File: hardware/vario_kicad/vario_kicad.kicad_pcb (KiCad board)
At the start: 4 copper layers, 70 x 50 mm, 94 parts, among them Q1 NMOS, Q2 PMOS, U2 BME280, U3 W25Q128JVS, U4 USB C connector, U5 STM32L072CBTx, Y1 Crystal, Y2 Crystal_GND24

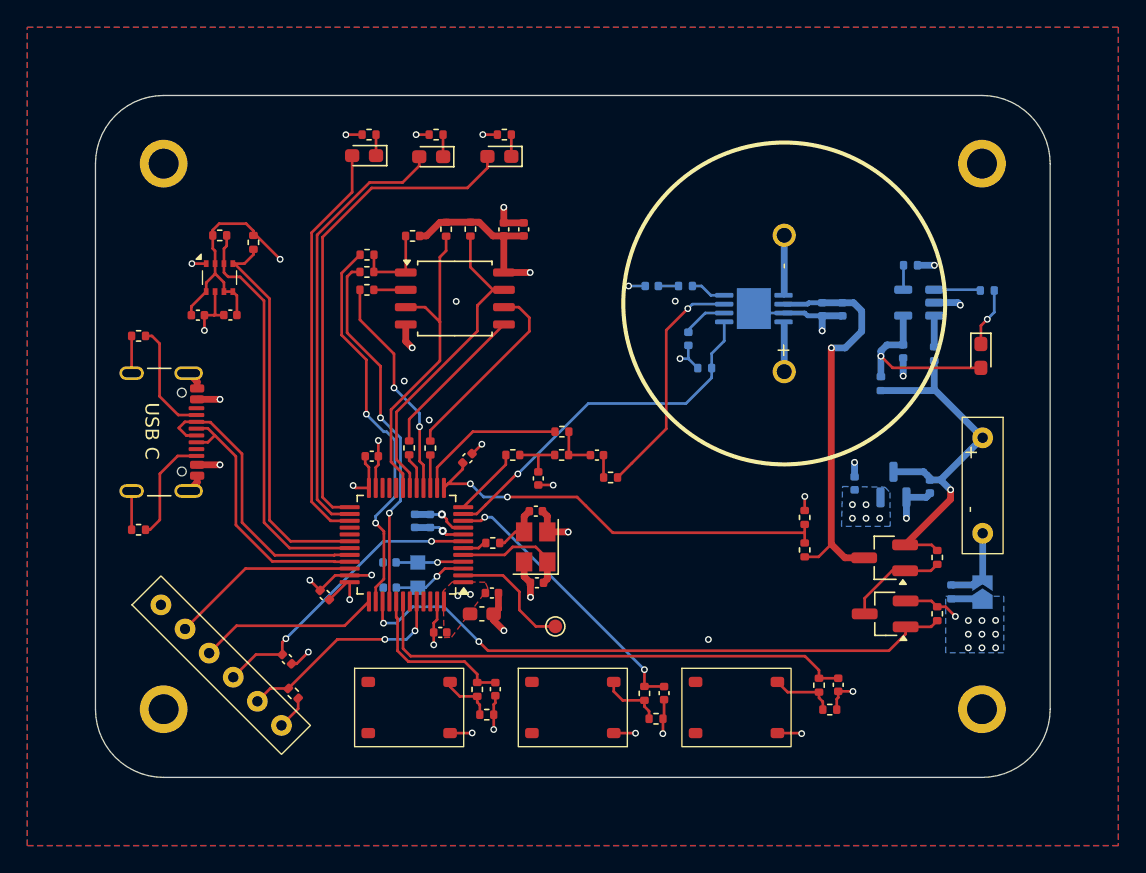
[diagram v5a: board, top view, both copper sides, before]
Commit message: modify silkscreen
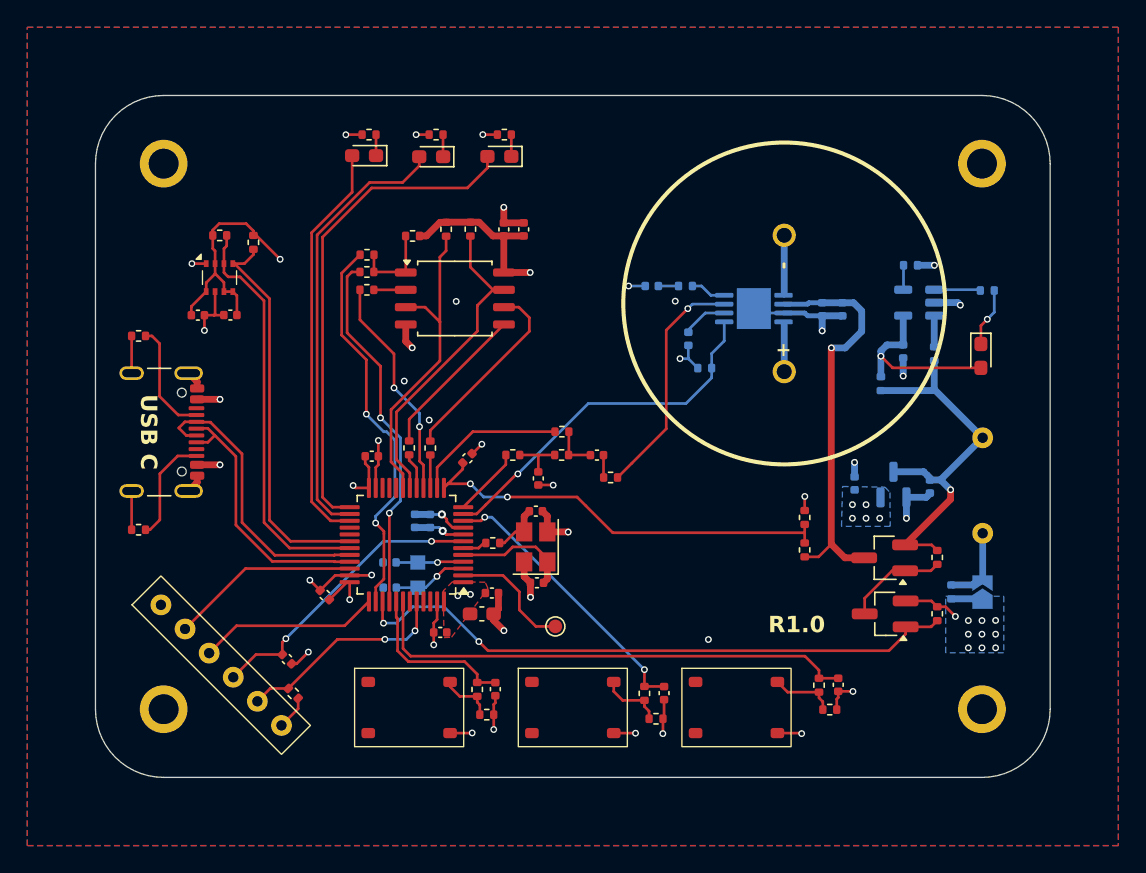
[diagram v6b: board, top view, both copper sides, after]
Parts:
- BT2: moved to B.Cu
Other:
- board text added: "R1.0"
- board text added: "github.com/vasilNnikolov/vario"
- board text removed: "github.com/vasilNnikolov/vario R1.0"
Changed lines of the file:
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@@
 				(font
 					(size 1 1)
-					(thickness 0.1)
+					(thickness 0.2)
+					(bold yes)
 				)
 				(justify left bottom)
@@
 				(font
 					(size 1 1)
-					(thickness 0.1)
+					(thickness 0.2)
+					(bold yes)
 				)
 				(justify left bottom)
@@
 		(tags "capacitor")
 		(property "Reference" "C13"
-			(at 0 -1.16 360)
+			(at 0 -1.16 0)
 			(layer "F.SilkS")
 			(hide yes)
@@
 		)
 		(property "Value" "12.5pF"
-			(at 0 1.16 360)
+			(at 0 1.16 0)
 			(layer "F.Fab")
 			(effects
@@
 		)
 		(fp_text user "${REFERENCE}"
-			(at 0 0 360)
+			(at 0 0 0)
 			(layer "F.Fab")
 			(effects
@@
 		(tags "capacitor")
 		(property "Reference" "C20"
-			(at 0 -1.16 360)
+			(at 0 -1.16 0)
 			(layer "F.SilkS")
 			(hide yes)
@@
 		)
 		(property "Value" "12.5pF"
-			(at 0 1.16 360)
+			(at 0 1.16 0)
 			(layer "F.Fab")
 			(effects
@@
 		)
 		(fp_text user "${REFERENCE}"
-			(at 0 0 360)
+			(at 0 0 0)
 			(layer "F.Fab")
 			(effects
@@
 		)
 		(fp_text user "USB C"
-			(at -2.5 8.5 -90)
+			(at -3.1 8.85 -90)
 			(unlocked yes)
 			(layer "F.SilkS")
 			(effects
 				(font
-					(size 1 1)
-					(thickness 0.1)
+					(size 1.2 1.2)
+					(thickness 0.2)
+					(bold yes)
 				)
 				(justify left bottom)
@@
 		)
 		(fp_text user "${REFERENCE}"
-			(at 0 2.5 -90)
+			(at 0 -2.5 -90)
 			(unlocked yes)
 			(layer "F.Fab")
@@
 		)
 		(fp_text user "${REFERENCE}"
-			(at 0 -2.5 -90)
+			(at 0 2.5 -90)
 			(unlocked yes)
 			(layer "F.Fab")
@@
 		)
 	)
-	(footprint "symbol_lib:battery_th"
-		(layer "F.Cu")
-		(at 165.05 128.6 -90)
-		(property "Reference" "BT2"
-			(at 0 -13.5 -90)
-			(unlocked yes)
-			(layer "F.SilkS")
-			(hide yes)
-			(effects
-				(font
-					(size 1 1)
-					(thickness 0.1)
-				)
-			)
-		)
-		(property "Value" "Battery_Cell"
-			(at 0 -12 -90)
-			(unlocked yes)
-			(layer "F.Fab")
-			(effects
-				(font
-					(size 1 1)
-					(thickness 0.15)
-				)
-			)
-		)
-		(property "Footprint" "symbol_lib:battery_th"
-			(at 0 -13 -90)
-			(unlocked yes)
-			(layer "F.Fab")
-			(hide yes)
-			(effects
-				(font
-					(size 1 1)
-					(thickness 0.15)
-				)
-			)
-		)
-		(property "Datasheet" ""
-			(at 0 -13 -90)
-			(unlocked yes)
-			(layer "F.Fab")
-			(hide yes)
-			(effects
-				(font
-					(size 1 1)
-					(thickness 0.15)
-				)
-			)
-		)
-		(property "Description" "Single-cell battery"
-			(at 0 -13 -90)
-			(unlocked yes)
-			(layer "F.Fab")
-			(hide yes)
-			(effects
-				(font
-					(size 1 1)
-					(thickness 0.15)
-				)
-			)
-		)
-		(property "Sim.Pins" ""
-			(at 0 0 -90)
-			(unlocked yes)
-			(layer "F.Fab")
-			(hide yes)
-			(effects
-				(font
-					(size 1 1)
-					(thickness 0.15)
-				)
-			)
-		)
-		(sheetname "power")
-		(sheetfile "power.kicad_sch")
-		(attr through_hole)
-		(fp_rect
-			(start -5 -1.5)
-			(end 5 1.5)
-			(stroke
-				(width 0.1)
-				(type default)
-			)
-			(fill none)
-			(layer "F.SilkS")
-		)
-		(fp_text user "+"
-			(at -3 1.4 -90)
-			(unlocked yes)
-			(layer "F.SilkS")
-			(effects
-				(font
-					(size 1 1)
-					(thickness 0.1)
-				)
-				(justify left bottom)
-			)
-		)
-		(fp_text user "-"
-			(at 1.5 1.4 -90)
-			(unlocked yes)
-			(layer "F.SilkS")
-			(effects
-				(font
-					(size 1 1)
-					(thickness 0.1)
-				)
-				(justify left bottom)
-			)
-		)
-		(fp_text user "${REFERENCE}"
-			(at 0 -10.5 -90)
-			(unlocked yes)
-			(layer "F.Fab")
-			(effects
-				(font
-					(size 1 1)
-					(thickness 0.15)
-				)
-			)
-		)
-		(pad "1" thru_hole circle
-			(at -3.5 0 270)
-			(size 1.524 1.524)
-			(drill 0.762)
-			(layers "*.Cu" "*.Mask" "In3.Cu" "In4.Cu" "In5.Cu" "In6.Cu" "In7.Cu" "In8.Cu"
-				"In9.Cu" "In10.Cu" "In11.Cu" "In12.Cu" "In13.Cu" "In14.Cu" "In15.Cu"
-				"In16.Cu" "In17.Cu" "In18.Cu" "In19.Cu" "In20.Cu" "In21.Cu" "In22.Cu"
-				"In23.Cu" "In24.Cu" "In25.Cu" "In26.Cu" "In27.Cu" "In28.Cu" "In29.Cu"
-				"In30.Cu"
-			)
-			(remove_unused_layers no)
-			(net 1 "VBATT")
-			(pinfunction "+")
-			(pintype "passive")
-		)
-		(pad "2" thru_hole circle
-			(at 3.5 0 270)
-			(size 1.524 1.524)
-			(drill 0.762)
-			(layers "*.Cu" "*.Mask" "In3.Cu" "In4.Cu" "In5.Cu" "In6.Cu" "In7.Cu" "In8.Cu"
-				"In9.Cu" "In10.Cu" "In11.Cu" "In12.Cu" "In13.Cu" "In14.Cu" "In15.Cu"
-				"In16.Cu" "In17.Cu" "In18.Cu" "In19.Cu" "In20.Cu" "In21.Cu" "In22.Cu"
-				"In23.Cu" "In24.Cu" "In25.Cu" "In26.Cu" "In27.Cu" "In28.Cu" "In29.Cu"
-				"In30.Cu"
-			)
-			(remove_unused_layers no)
-			(net 58 "Net-(BT2--)")
-			(pinfunction "-")
-			(pintype "passive")
-		)
-	)
 	(footprint "Capacitor_SMD:C_0402_1005Metric"
 		(layer "F.Cu")
@@
 			(at 0 1.17 90)
 			(layer "B.SilkS")
+			(hide yes)
 			(effects
 				(font
@@
 		)
 	)
+	(footprint "symbol_lib:battery_th"
+		(layer "B.Cu")
+		(at 165.05 128.6 -90)
+		(property "Reference" "BT2"
+			(at 0 13.5 90)
+			(unlocked yes)
+			(layer "B.SilkS")
+			(hide yes)
+			(effects
+				(font
+					(size 1 1)
+					(thickness 0.1)
+				)
+				(justify mirror)
+			)
+		)
+		(property "Value" "Battery_Cell"
+			(at 0 12 90)
+			(unlocked yes)
+			(layer "B.Fab")
+			(effects
+				(font
+					(size 1 1)
+					(thickness 0.15)
+				)
+				(justify mirror)
+			)
+		)
+		(property "Footprint" "symbol_lib:battery_th"
+			(at 0 13 90)
+			(unlocked yes)
+			(layer "B.Fab")
+			(hide yes)
+			(effects
+				(font
+					(size 1 1)
+					(thickness 0.15)
+				)
+				(justify mirror)
+			)
+		)
+		(property "Datasheet" ""
+			(at 0 13 90)
+			(unlocked yes)
+			(layer "B.Fab")
+			(hide yes)
+			(effects
+				(font
+					(size 1 1)
+					(thickness 0.15)
+				)
+				(justify mirror)
+			)
+		)
+		(property "Description" "Single-cell battery"
+			(at 0 13 90)
+			(unlocked yes)
+			(layer "B.Fab")
+			(hide yes)
+			(effects
+				(font
+					(size 1 1)
+					(thickness 0.15)
+				)
+				(justify mirror)
+			)
+		)
+		(sheetname "power")
+		(sheetfile "power.kicad_sch")
+		(attr through_hole)
+		(fp_rect
+			(start -5 1.5)
+			(end 5 -1.5)
+			(stroke
+				(width 0.2)
+				(type default)
+			)
+			(fill none)
+			(layer "B.SilkS")
+		)
+		(fp_text user "-"
+			(at 1.15 -1.3 90)
+			(unlocked yes)
+			(layer "B.SilkS")
+			(effects
+				(font
+					(size 1.2 1.2)
+					(thickness 0.2)
+					(bold yes)
+				)
+				(justify left bottom mirror)
+			)
+		)
+		(fp_text user "+"
+			(at -2.85 -1.3 90)
+			(unlocked yes)
+			(layer "B.SilkS")
+			(effects
+				(font
+					(size 1.2 1.2)
+					(thickness 0.2)
+					(bold yes)
+				)
+				(justify left bottom mirror)
+			)
+		)
+		(fp_text user "${REFERENCE}"
+			(at 0 10.5 90)
+			(unlocked yes)
+			(layer "B.Fab")
+			(effects
+				(font
+					(size 1 1)
+					(thickness 0.15)
+				)
+				(justify mirror)
+			)
+		)
+		(pad "1" thru_hole circle
+			(at -3.5 0 270)
+			(size 1.524 1.524)
+			(drill 0.762)
+			(layers "*.Cu" "*.Mask" "In3.Cu" "In4.Cu" "In5.Cu" "In6.Cu" "In7.Cu" "In8.Cu"
+				"In9.Cu" "In10.Cu" "In11.Cu" "In12.Cu" "In13.Cu" "In14.Cu" "In15.Cu"
+				"In16.Cu" "In17.Cu" "In18.Cu" "In19.Cu" "In20.Cu" "In21.Cu" "In22.Cu"
+				"In23.Cu" "In24.Cu" "In25.Cu" "In26.Cu" "In27.Cu" "In28.Cu" "In29.Cu"
+				"In30.Cu"
+			)
+			(remove_unused_layers no)
+			(net 1 "VBATT")
+			(pinfunction "+")
+			(pintype "passive")
+		)
+		(pad "2" thru_hole circle
+			(at 3.5 0 270)
+			(size 1.524 1.524)
+			(drill 0.762)
+			(layers "*.Cu" "*.Mask" "In3.Cu" "In4.Cu" "In5.Cu" "In6.Cu" "In7.Cu" "In8.Cu"
+				"In9.Cu" "In10.Cu" "In11.Cu" "In12.Cu" "In13.Cu" "In14.Cu" "In15.Cu"
+				"In16.Cu" "In17.Cu" "In18.Cu" "In19.Cu" "In20.Cu" "In21.Cu" "In22.Cu"
+				"In23.Cu" "In24.Cu" "In25.Cu" "In26.Cu" "In27.Cu" "In28.Cu" "In29.Cu"
+				"In30.Cu"
+			)
+			(remove_unused_layers no)
+			(net 58 "Net-(BT2--)")
+			(pinfunction "-")
+			(pintype "passive")
+		)
+	)
 	(footprint "Capacitor_SMD:C_0402_1005Metric"
 		(layer "B.Cu")
@@
 		(layer "Edge.Cuts")
 	)
-	(gr_text "github.com/vasilNnikolov/vario\nR1.0"
-		(at 136.28 146.31 0)
+	(gr_text "github.com/vasilNnikolov/vario"
+		(at 149.58 145.16 0)
 		(layer "B.SilkS")
 		(effects
 			(font
-				(size 0.5 0.5)
-				(thickness 0.1)
+				(size 1.2 1.2)
+				(thickness 0.2)
+				(bold yes)
 			)
 			(justify left bottom mirror)
 		)
 	)
+	(gr_text "R1.0"
+		(at 149.32 139.5 0)
+		(layer "F.SilkS")
+		(effects
+			(font
+				(size 1.2 1.2)
+				(thickness 0.2)
+				(bold yes)
+			)
+			(justify left bottom)
+		)
+	)

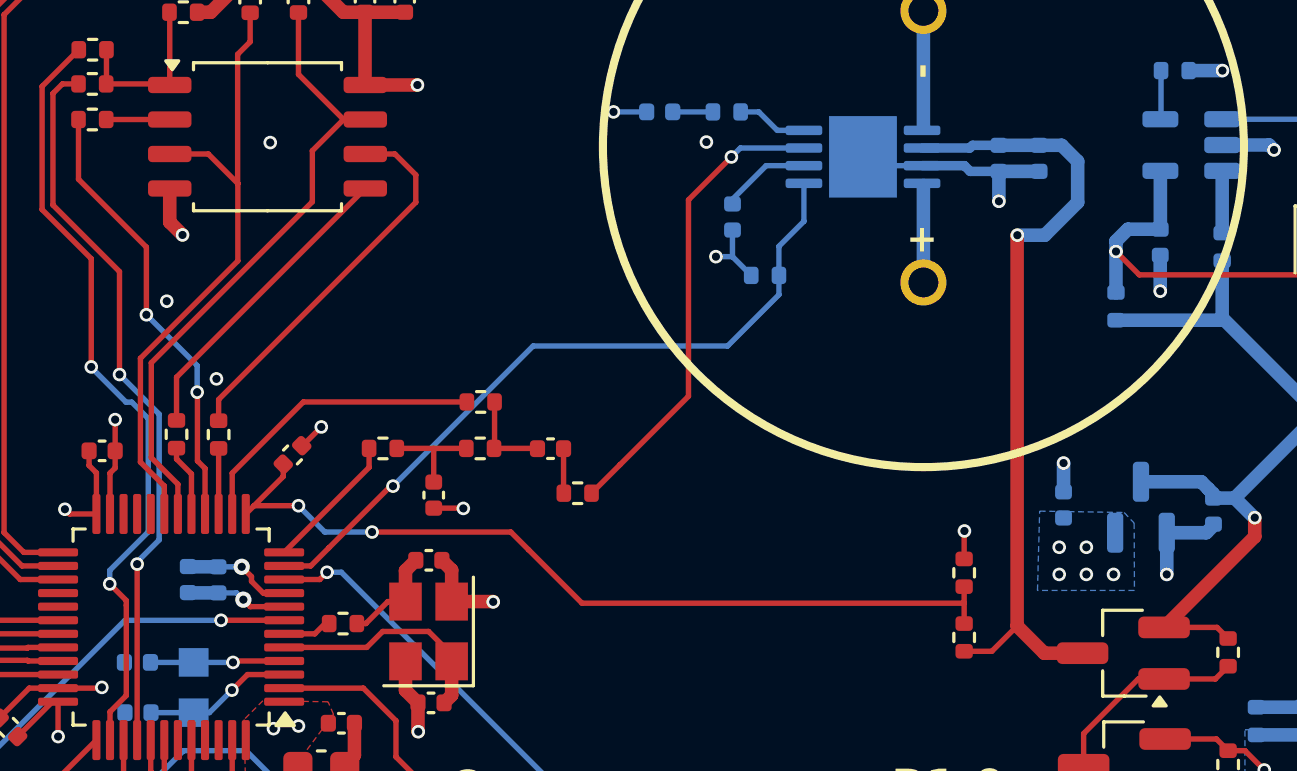
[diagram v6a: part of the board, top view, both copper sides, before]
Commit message: finished board variant 1, LSE on bottom
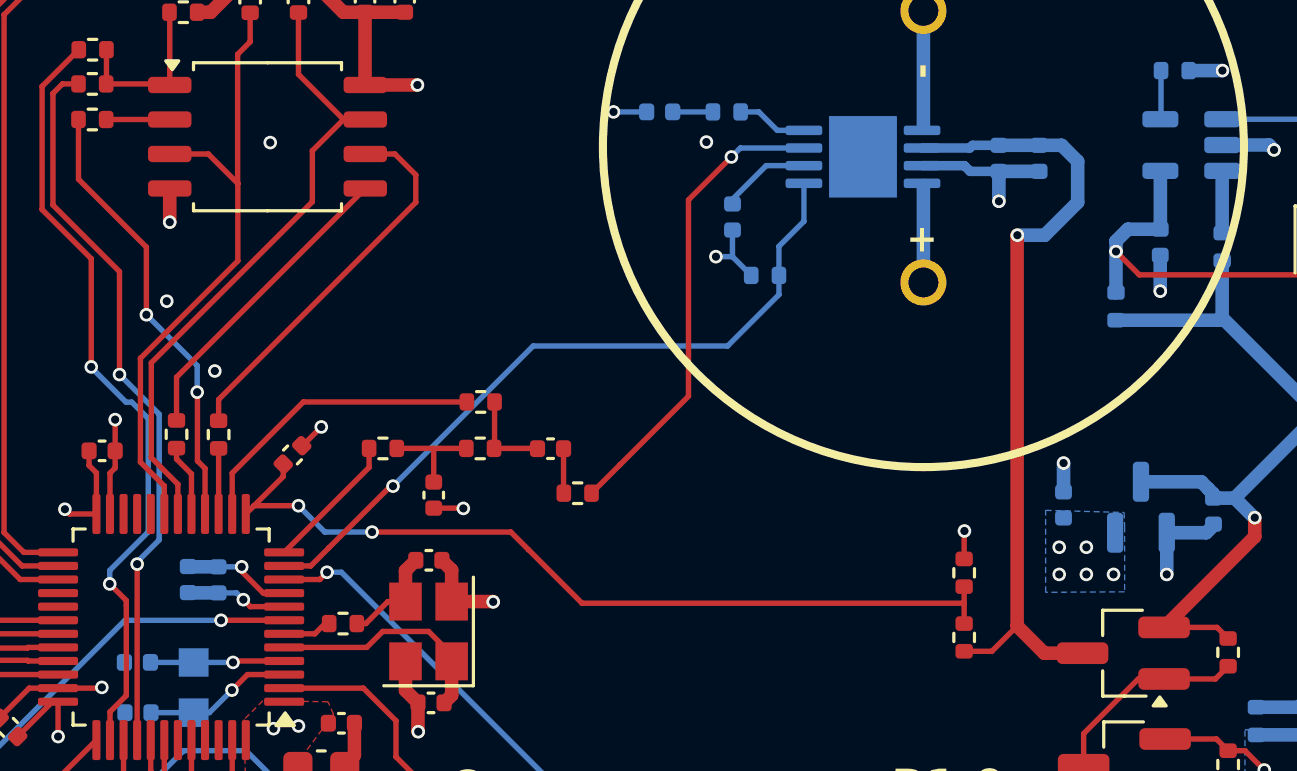
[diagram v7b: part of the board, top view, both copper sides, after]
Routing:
- net GND: track 87.9 -> 85.4 mm
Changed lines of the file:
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@@
 			(drillshape 0)
 			(scaleselection 1)
-			(outputdirectory "")
+			(outputdirectory "fabrication/")
 		)
 	)
@@
 	)
 	(segment
-		(start 122.75 116.79)
-		(end 122.75 118.03)
-		(width 0.5)
-		(layer "F.Cu")
-		(net 2)
-	)
-	(segment
 		(start 141.69 144.3)
 		(end 141.69 145.62)
@@
 	)
 	(segment
-		(start 122.75 118.03)
-		(end 123.22 118.5)
-		(width 0.5)
-		(layer "F.Cu")
-		(net 2)
-	)
-	(segment
 		(start 114.860624 144.967046)
 		(end 114.860624 144.200624)
@@
 	)
 	(segment
+		(start 122.75 118.03)
+		(end 122.75 116.79)
+		(width 0.5)
+		(layer "F.Cu")
+		(net 2)
+	)
+	(segment
 		(start 154.46 144.15)
 		(end 154.35 144.26)
@@
 	)
 	(via
-		(at 123.22 118.5)
+		(at 122.75 118.03)
 		(size 0.5)
 		(drill 0.3)
@@
 	)
 	(via
-		(at 124.47 123.8)
+		(at 124.41 123.51)
 		(size 0.5)
 		(drill 0.3)
@@
 	(via
 		(at 125.46 131.93)
-		(size 0.6)
+		(size 0.5)
 		(drill 0.3)
 		(layers "F.Cu" "B.Cu")
@@
 	)
 	(segment
-		(start 150.45 115.95)
-		(end 148.6 115.95)
-		(width 0.2)
-		(layer "B.Cu")
-		(net 2)
-	)
-	(segment
 		(start 162.76 136.91)
 		(end 164.45 136.91)
@@
 	)
 	(segment
-		(start 120.05 128.775)
-		(end 120.05 127.26)
+		(start 126.19259 131.6875)
+		(end 126.9625 131.6875)
 		(width 0.2)
 		(layer "F.Cu")
@@
 	)
 	(segment
-		(start 125.4 130.72)
-		(end 125.76 131.08)
+		(start 120.05 128.775)
+		(end 120.05 127.26)
 		(width 0.2)
 		(layer "F.Cu")
@@
 	)
 	(segment
-		(start 126.19259 131.6875)
-		(end 126.9625 131.6875)
-		(width 0.2)
-		(layer "F.Cu")
-		(net 3)
-	)
-	(segment
 		(start 109.42 114.38)
 		(end 110.07 114.38)
@@
 	)
 	(segment
-		(start 125.76 131.08)
-		(end 125.76 131.25491)
-		(width 0.2)
-		(layer "F.Cu")
-		(net 3)
-	)
-	(segment
 		(start 128.13 109.29)
 		(end 127.49 109.29)
@@
 	)
 	(segment
-		(start 125.76 131.25491)
-		(end 126.19259 131.6875)
-		(width 0.2)
-		(layer "F.Cu")
-		(net 3)
-	)
-	(segment
 		(start 111.58 109.93)
 		(end 111.58 110.26)
@@
 	)
 	(segment
+		(start 125.4 130.72)
+		(end 125.4 130.89491)
+		(width 0.2)
+		(layer "F.Cu")
+		(net 3)
+	)
+	(segment
 		(start 109.42 113.71)
 		(end 109.42 114.38)
@@
 	)
 	(segment
+		(start 125.4 130.89491)
+		(end 126.19259 131.6875)
+		(width 0.2)
+		(layer "F.Cu")
+		(net 3)
+	)
+	(segment
 		(start 129.14 110.3)
 		(end 128.13 109.29)
@@
 	(via
 		(at 125.4 130.72)
-		(size 0.6)
+		(size 0.5)
 		(drill 0.3)
 		(layers "F.Cu" "B.Cu")
@@
 		(name "VCC input")
 		(hatch none 0.5)
-		(connect_pads
+		(connect_pads yes
 			(clearance 0.25)
 		)
@@
 		(polygon
 			(pts
-				(xy 154.78 128.67) (xy 157.89 128.72) (xy 158.26 129.11) (xy 158.27 131.59) (xy 154.7 131.59)
+				(xy 155 128.64) (xy 157.89 128.72) (xy 157.91 129.23) (xy 157.91 131.64) (xy 155 131.66)
 			)
 		)
